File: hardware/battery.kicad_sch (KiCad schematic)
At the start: 23 parts, among them J2 B2B-XH-A, J3 PRPC001DAAN-RC, Q2 DMG2305UX-7, Q3 DMN2005UFG, Q4 DMN2005UFG, U2 BQ29728DSER, U3 MCP73833T-FCI/MF

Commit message: HW: Refine schematic
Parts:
- C5: footprint Capacitor_SMD:CP_Elec_6.3x5.4 -> Capacitor_THT:CP_Radial_D5.0mm_P2.00mm; DigiKey Part Number 732-8419-1-ND -> 732-8598-1-ND; MPN (none) -> 860010372006; Manufacturer (none) -> Würth Elektronik
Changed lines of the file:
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@@
 			)
 		)
-		(property "Footprint" "Capacitor_SMD:CP_Elec_6.3x5.4"
+		(property "Footprint" "Capacitor_THT:CP_Radial_D5.0mm_P2.00mm"
 			(at 128.5748 71.12 0)
 			(effects
@@
 			)
 		)
-		(property "DigiKey Part Number" "732-8419-1-ND"
+		(property "DigiKey Part Number" "732-8598-1-ND"
 			(at 129.54 67.31 0)
 			(effects
@@
 			)
 		)
-		(property "MPN" ""
+		(property "MPN" "860010372006"
 			(at 129.54 67.31 0)
 			(effects
@@
 			)
 		)
-		(property "Manufacturer" ""
+		(property "Manufacturer" "Würth Elektronik"
 			(at 129.54 67.31 0)
 			(effects

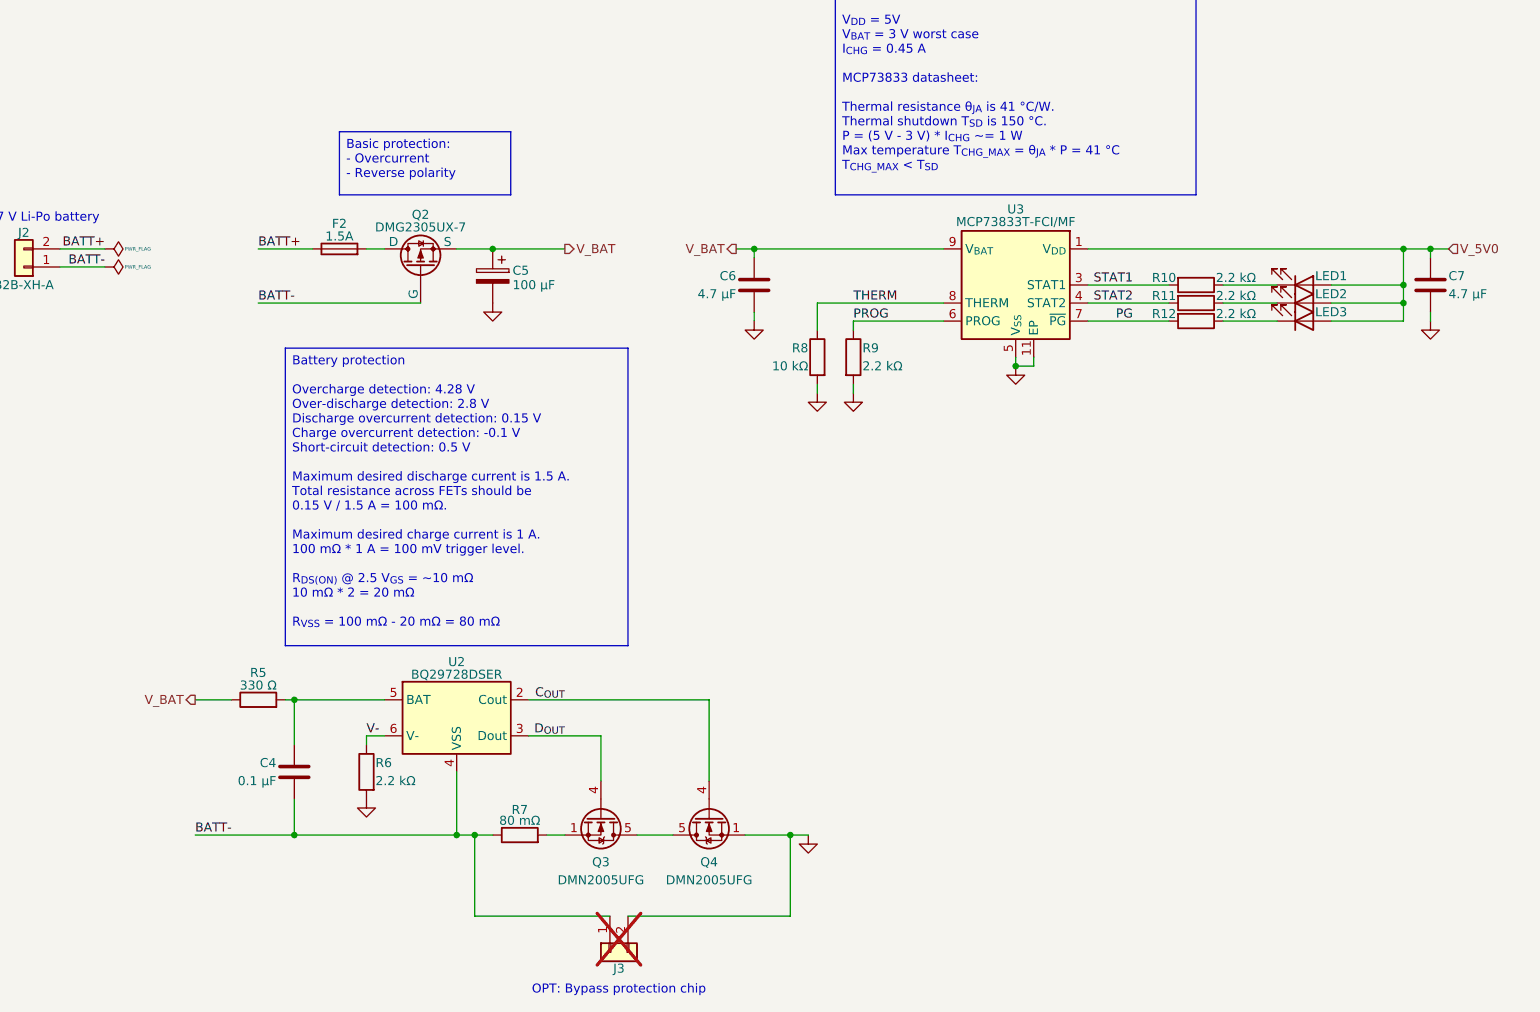
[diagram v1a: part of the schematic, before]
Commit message: HW: Fill BOM and refine schema
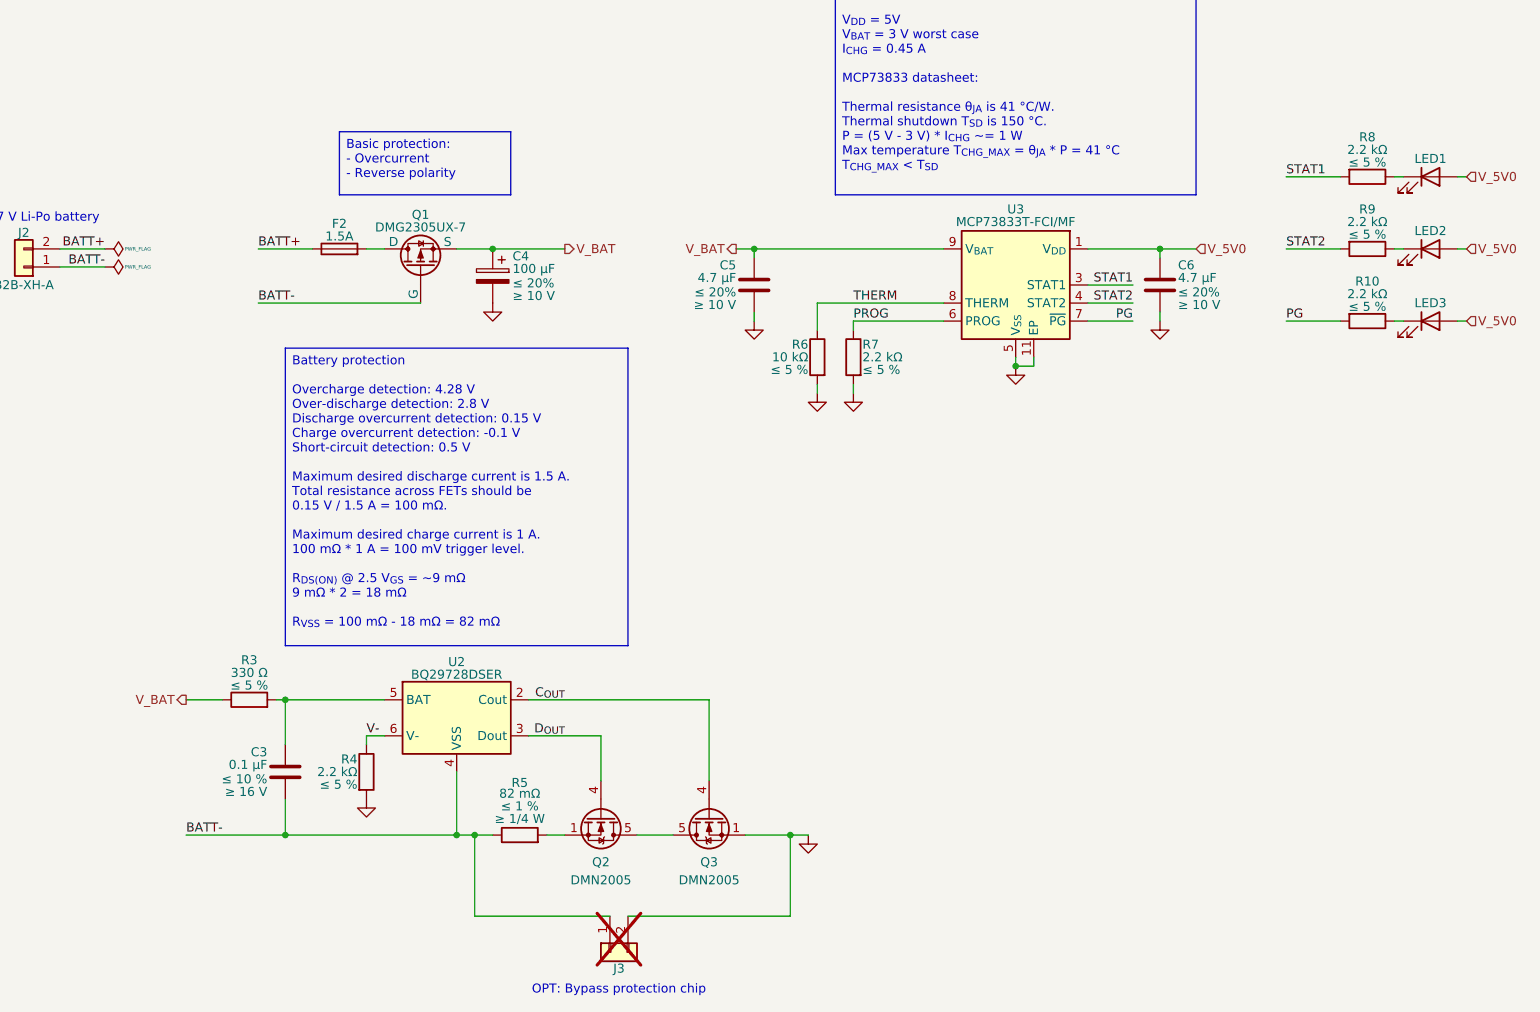
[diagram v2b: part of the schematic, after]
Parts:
- removed C4: 0.1 µF, Capacitor_SMD:C_0402_1005Metric, symbol Device:C
- removed C7: 4.7 µF, Capacitor_SMD:C_0402_1005Metric, symbol Device:C
- removed R11, R12: 2.2 kΩ, Resistor_SMD:R_0402_1005Metric, symbol Device:R
- added C3: 0.1 µF, Capacitor_SMD:C_0402_1005Metric, symbol Device:C
- added C6: 4.7 µF, Capacitor_SMD:C_0402_1005Metric, symbol Device:C
- added R7, R8: 2.2 kΩ, Resistor_SMD:R_0402_1005Metric, symbol Device:R
- C4: renamed from C5; Class (none) -> AlumElec; Footprint review check (none) -> +; Size (none) -> 5.0mmx2.0mm; Tolerance (none) -> ≤ 20%; Voltage (none) -> ≥ 10 V
- C5: renamed from C6; Class (none) -> X5R; DigiKey Part Number (none) -> 490-14306-1-ND; Footprint review check (none) -> +; MPN (none) -> GRM155R61A475MEAAD; Manufacturer (none) -> Murata Electronics; Size (none) -> 0402; Tolerance (none) -> ≤ 20%; Voltage (none) -> ≥ 10 V
- F2: DigiKey Part Number (none) -> 283-PTSLR08056V150CT-ND
- J2: DigiKey Part Number (none) -> 455-B2B-XH-A-ND; Footprint review check (none) -> +
- LED1, LED2, LED3: DigiKey Part Number (none) -> 732-5000-1-ND
- Q1: renamed from Q2; DigiKey Part Number (none) -> DMG2305UX-7DICT-ND
- Q2: renamed from Q3; value DMN2005UFG -> DMN2005; DigiKey Part Number (none) -> DMN2005UFG-7DICT-ND; Footprint review check (none) -> +; MPN (none) -> DMN2005UFG-7; Manufacturer (none) -> Diodes Incorporated
- Q3: renamed from Q4; value DMN2005UFG -> DMN2005; DigiKey Part Number (none) -> DMN2005UFG-7DICT-ND; Footprint review check (none) -> +; MPN (none) -> DMN2005UFG-7; Manufacturer (none) -> Diodes Incorporated
- R10, R9: DigiKey Part Number (none) -> 732-560112110087CT-ND; Footprint review check (none) -> +; MPN (none) -> 560112110087; Manufacturer (none) -> Würth Elektronik; Tolerance (none) -> ≤ 5 %
- R3: renamed from R5; DigiKey Part Number (none) -> 732-560112110231CT-ND; Footprint review check (none) -> +; MPN (none) -> 560112110231; Manufacturer (none) -> Würth Elektronik; Tolerance (none) -> ≤ 5 %
- R4: renamed from R6; DigiKey Part Number (none) -> 732-560112110087CT-ND; Footprint review check (none) -> +; MPN (none) -> 560112110087; Manufacturer (none) -> Würth Elektronik; Tolerance (none) -> ≤ 5 %
- R5: renamed from R7; value 80 mΩ -> 82 mΩ; DigiKey Part Number (none) -> 13-RL1206FR-070R082LCT-ND; Footprint review check (none) -> +; MPN (none) -> RL1206FR-070R082L; Manufacturer (none) -> YAGEO; Power (none) -> ≥ 1/4 W; Tolerance (none) -> ≤ 1 %
- R6: renamed from R8; DigiKey Part Number (none) -> 732-560112110020CT-ND; Footprint review check (none) -> +; MPN (none) -> 560112110020; Manufacturer (none) -> Würth Elektronik; Tolerance (none) -> ≤ 5 %
- U2: DigiKey Part Number (none) -> 296-BQ29728DSERCT-ND
- U3: DigiKey Part Number (none) -> MCP73833T-FCI/MF
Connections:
- net BATT-: now also C3.2
- net GND: now also C6.2, R7.2; no longer R9.2
- net PG: now also R10.2
- net PROG: now also R7.1; no longer R9.1
- net STAT1: now also R8.2; no longer R10.2
- net STAT2: now also R9.2
- net V_5V0: now also C6.1
- net at LED1.1 (K): now also R8.1; no longer R10.1
- net at LED2.1 (K): now also R9.1
- net at LED3.1 (K): now also R10.1
- net at R3.2, U2.5 (BAT): now also C3.1
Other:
- moved on the sheet: LED1, R3

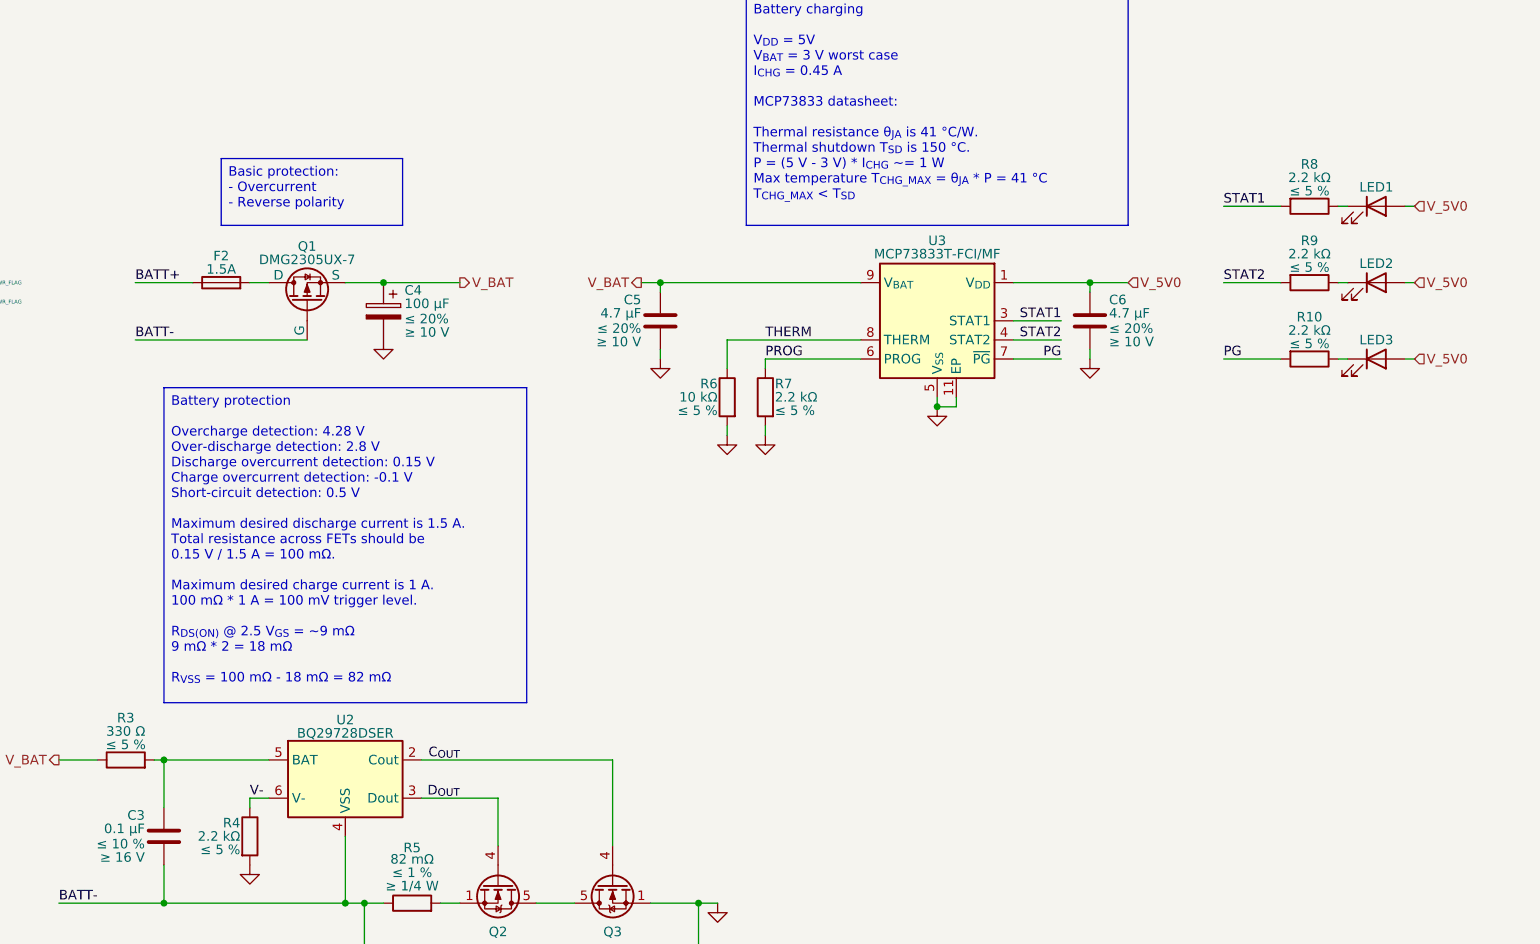
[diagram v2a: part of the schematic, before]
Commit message: HW: Add test points
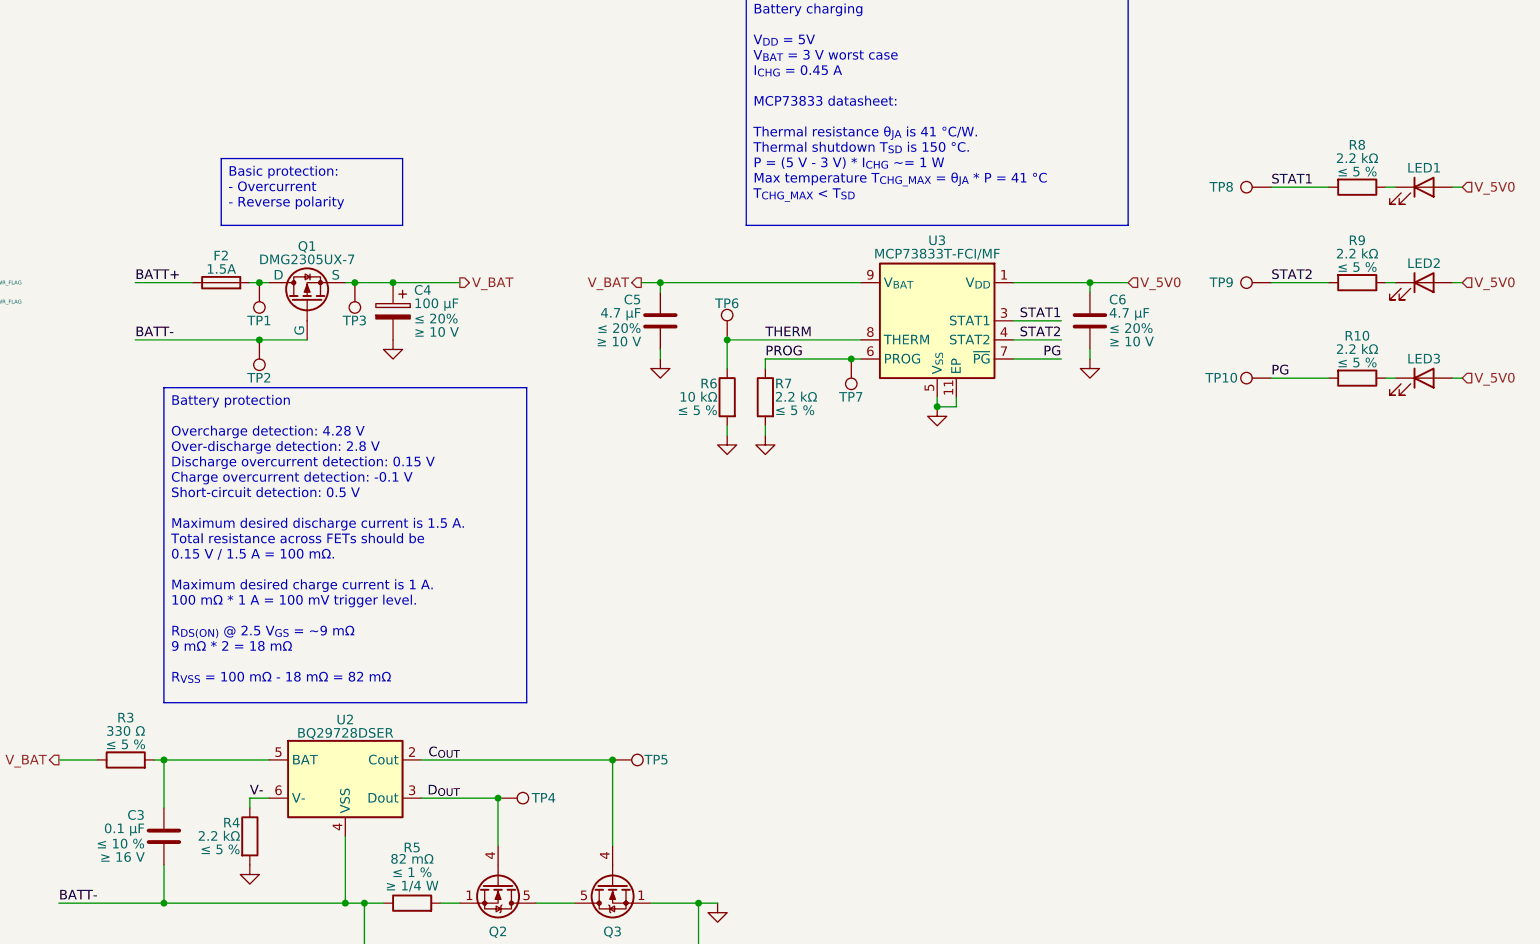
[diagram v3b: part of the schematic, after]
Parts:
- added TP1, TP10, TP2, TP3, TP4, TP5, TP6, TP7, TP8, TP9: TestPoint, TestPoint:TestPoint_Pad_D1.0mm, symbol Connector:TestPoint
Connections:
- net BATT-: now also TP2.1
- net C_{OUT}: now also TP5.1
- net D_{OUT}: now also TP4.1
- net PG: now also TP10.1
- net PROG: now also TP7.1
- net STAT1: now also TP8.1
- net STAT2: now also TP9.1
- net THERM: now also TP6.1
- net V_BAT: now also TP3.1
- net at F2.2, Q1.3 (D): now also TP1.1
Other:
- moved on the sheet: C4, LED1, LED2, LED3, R10, R8, R9

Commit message: HW: Section schematics
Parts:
- renumbered C4 to C3, C3 to C4
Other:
- note added: "A 3.7 V nominal LiPo battery can be used to power the device. The device nominally consumes from 10 mA (sleep) to 500 mA (data transmit) when battery powered. The charging current is 450 mA, so connect a battery with ≥ 450 mAh capacity. When powered by the USB-C, the battery can be charged."
- note added: "As LiPo batteries can be explosive, ensure that we are protected against: - Over-current charge - Over-current discharge - Over-voltage - Under-voltage - Reverse polarity - Short circuit"
- note added: "To ensure support for a wide variety of LiPo batteries, set the charging current to 450 mA. To visually confirm that charging is happening and that the battery is being used, LEDs are used according to the "STATUS OUTPUTS" table."
- note removed: "Input: 3.7 V Li-Po battery"
- moved on the sheet: C3, C4, C5, C6, F2, J2, J3, LED1, LED2, LED3, Q1, Q2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
